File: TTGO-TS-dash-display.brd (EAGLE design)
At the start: 42.9 x 30.5 mm, 35 parts, among them U8 NCP1117LPST50T3G

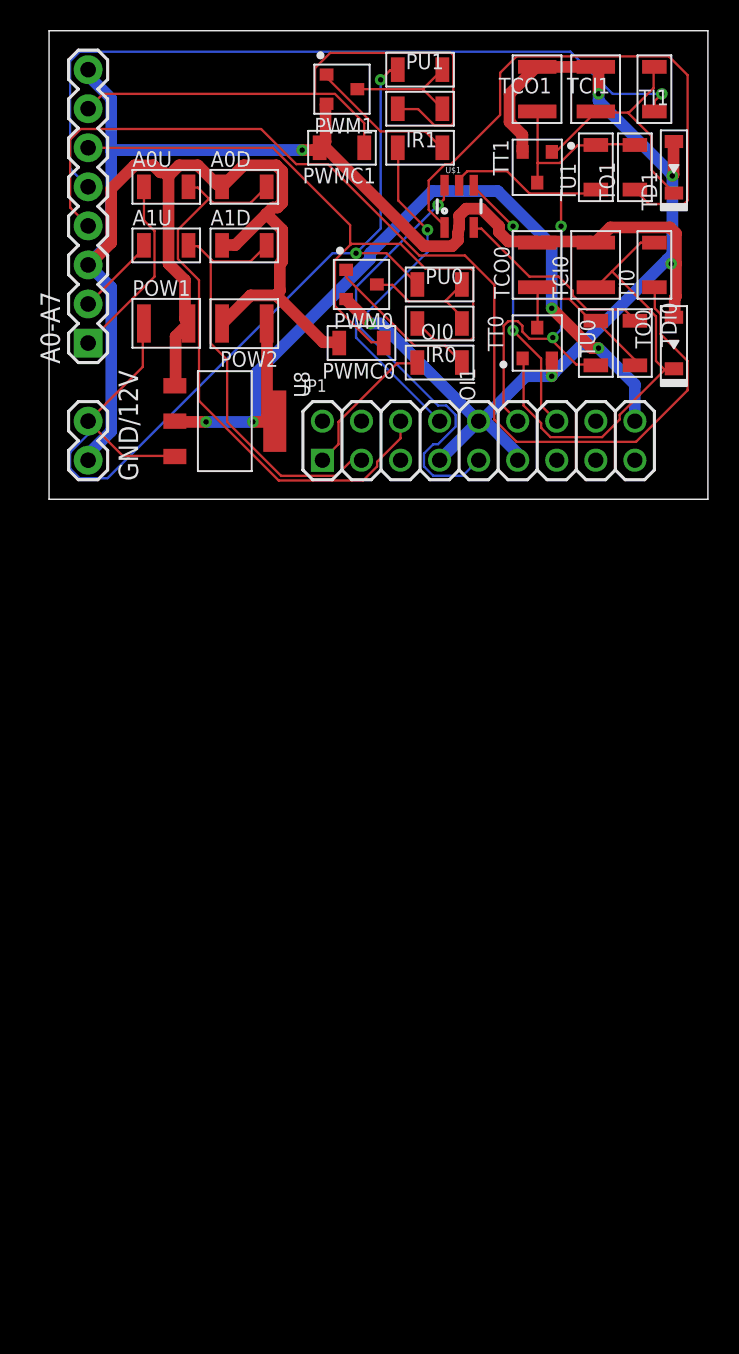
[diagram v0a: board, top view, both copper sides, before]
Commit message: Tinkering with expected changes for dash-mount board
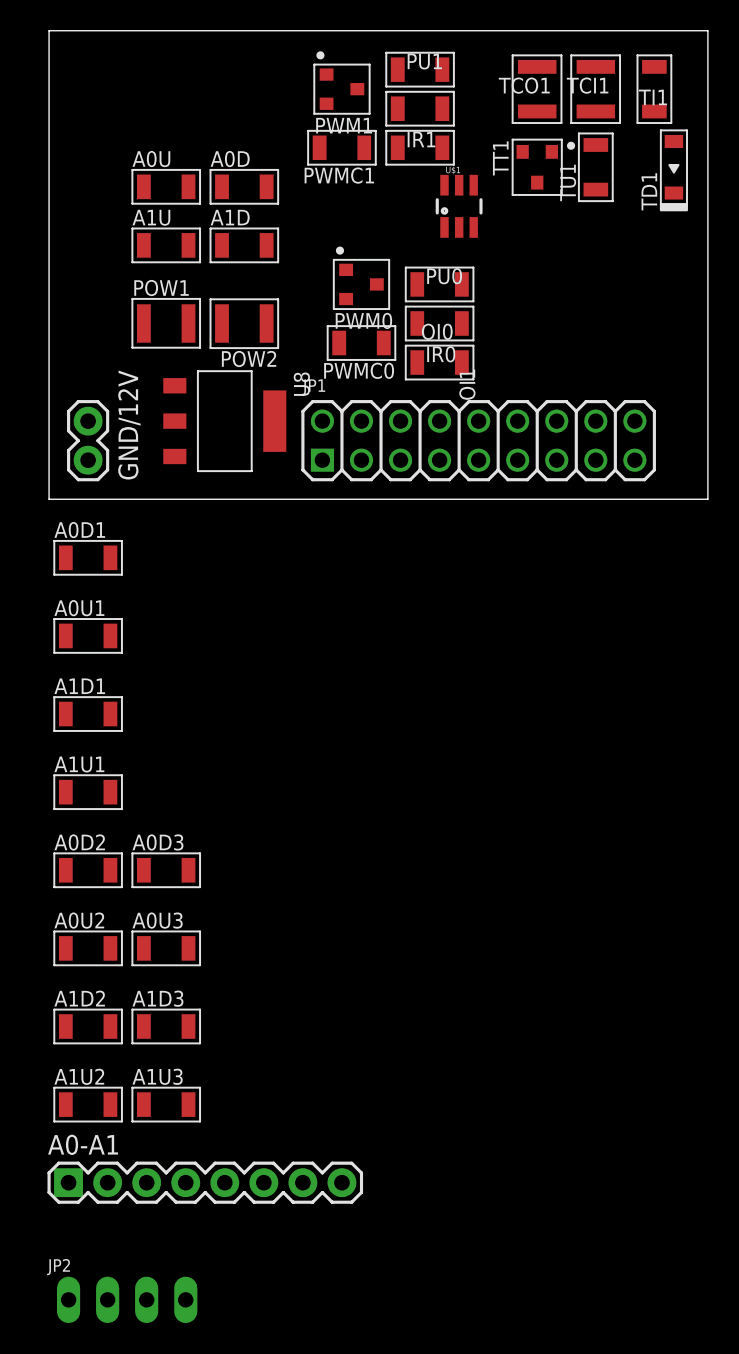
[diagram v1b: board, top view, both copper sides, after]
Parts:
- removed A0-A7: MF-CON-2.54mm-01x08, SparkFun-Connectors:1X08
- removed TCI0, TCO0: (no value), MF_Passives:C1210
- removed TDI0: MF-DIO-SOD123-1N4148, MF_Discrete_Semiconductor:SOD-123
- removed TI0, TO0, TO1, TU0: (no value), MF_Passives:R1206
- removed TT0: MF-DSC-SOT233-MMBT3904, MF_Discrete_Semiconductor:SOT-23-3
- added A0-A1: MF-CON-2.54mm-01x08, SparkFun-Connectors:1X08
- added A0D1, A0D2, A0D3, A0U1, A0U2, A0U3, A1D1, A1D2, A1D3, A1U1, A1U2, A1U3: (no value), MF_Passives:R1206
- added JP2: (no value), 00jim:1X04_OVAL
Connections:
- removed net D1: JP1.8, U$1.6
- removed net HV_D1: A0-A7.5, TI1.P$1
- removed net IO21_D4: TCO0.P$1, TO0.P$2, TT0.P$3, TU0.P$2
- removed net N$2: TCI0.P$1, TDI0.CATHODE, TI0.P$2, TT0.P$1
- removed net N$8: TO1.P$1, U$1.1
- removed net N$9: TO0.P$1, U$1.3
- new net A2: A0D1.P$2, A0U1.P$2
- new net A3: A1D1.P$2, A1U1.P$2
- new net A4: A0D2.P$2, A0U2.P$2
- new net A5: A1D2.P$2, A1U2.P$2
- new net A6: A0D3.P$2, A0U3.P$2
- new net A7: A1D3.P$2, A1U3.P$2
- new net HV-A2: A0-A1.3, A0U1.P$1
- new net HV-A3: A0-A1.4, A1U1.P$1
- new net HV-A4: A0-A1.5, A0U2.P$1
- new net HV-A5: A0-A1.6, A1U2.P$1
- new net HV-A6: A0-A1.7, A0U3.P$1
- new net HV-A7: A0-A1.8
- net D0: now also JP1.8; no longer JP1.14
- net GND: now also A0D1.P$1, A0D2.P$1, A0D3.P$1, A1D1.P$1, A1D2.P$1, A1D3.P$1, JP2.1; no longer A0-A7.3, A0-A7.8, TCI0.P$2, TCO0.P$2, TDI0.ANODE, TT0.P$2
- net HV-A0: now also A0-A1.1; no longer A0-A7.1
- net HV-A1: now also A0-A1.2; no longer A0-A7.2
- net HV_D0: now also JP2.4, TI1.P$1; no longer A0-A7.4, TI0.P$1
- net IO21_D1: now also U$1.1; no longer TO1.P$2
- net PWM0_HV: now also JP2.3; no longer A0-A7.6
- net PWM1_HV: now also JP2.2; no longer A0-A7.7
- net RAW: now also A1U3.P$1
- net VCC_33: no longer TU0.P$1
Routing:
- net GND: track 201.0 -> 0.00 mm, vias 6 -> 0
- net HV_D0: track 69.1 -> 0.00 mm
- net RAW: track 61.2 -> 0.00 mm, vias 2 -> 0
- net VCC: track 56.2 -> 0.00 mm, vias 4 -> 0
- net HV_D1: track 49.9 -> 0.00 mm, vias 1 -> 0
- net PWM0_HV: track 46.2 -> 0.00 mm
- net PWM1_HV: track 40.4 -> 0.00 mm
- net A0: track 38.2 -> 0.00 mm
- net N$8: track 37.9 -> 0.00 mm
- net VCC_33: track 34.1 -> 0.00 mm, vias 2 -> 0
- net PWM1: track 31.5 -> 0.00 mm, vias 1 -> 0
- net N$2: track 28.8 -> 0.00 mm
- net A1: track 27.6 -> 0.00 mm
- net D1: track 20.0 -> 0.00 mm, vias 1 -> 0
- net D0: track 17.6 -> 0.00 mm, vias 2 -> 0
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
